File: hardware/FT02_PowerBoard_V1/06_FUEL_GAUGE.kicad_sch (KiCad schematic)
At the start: 0 parts

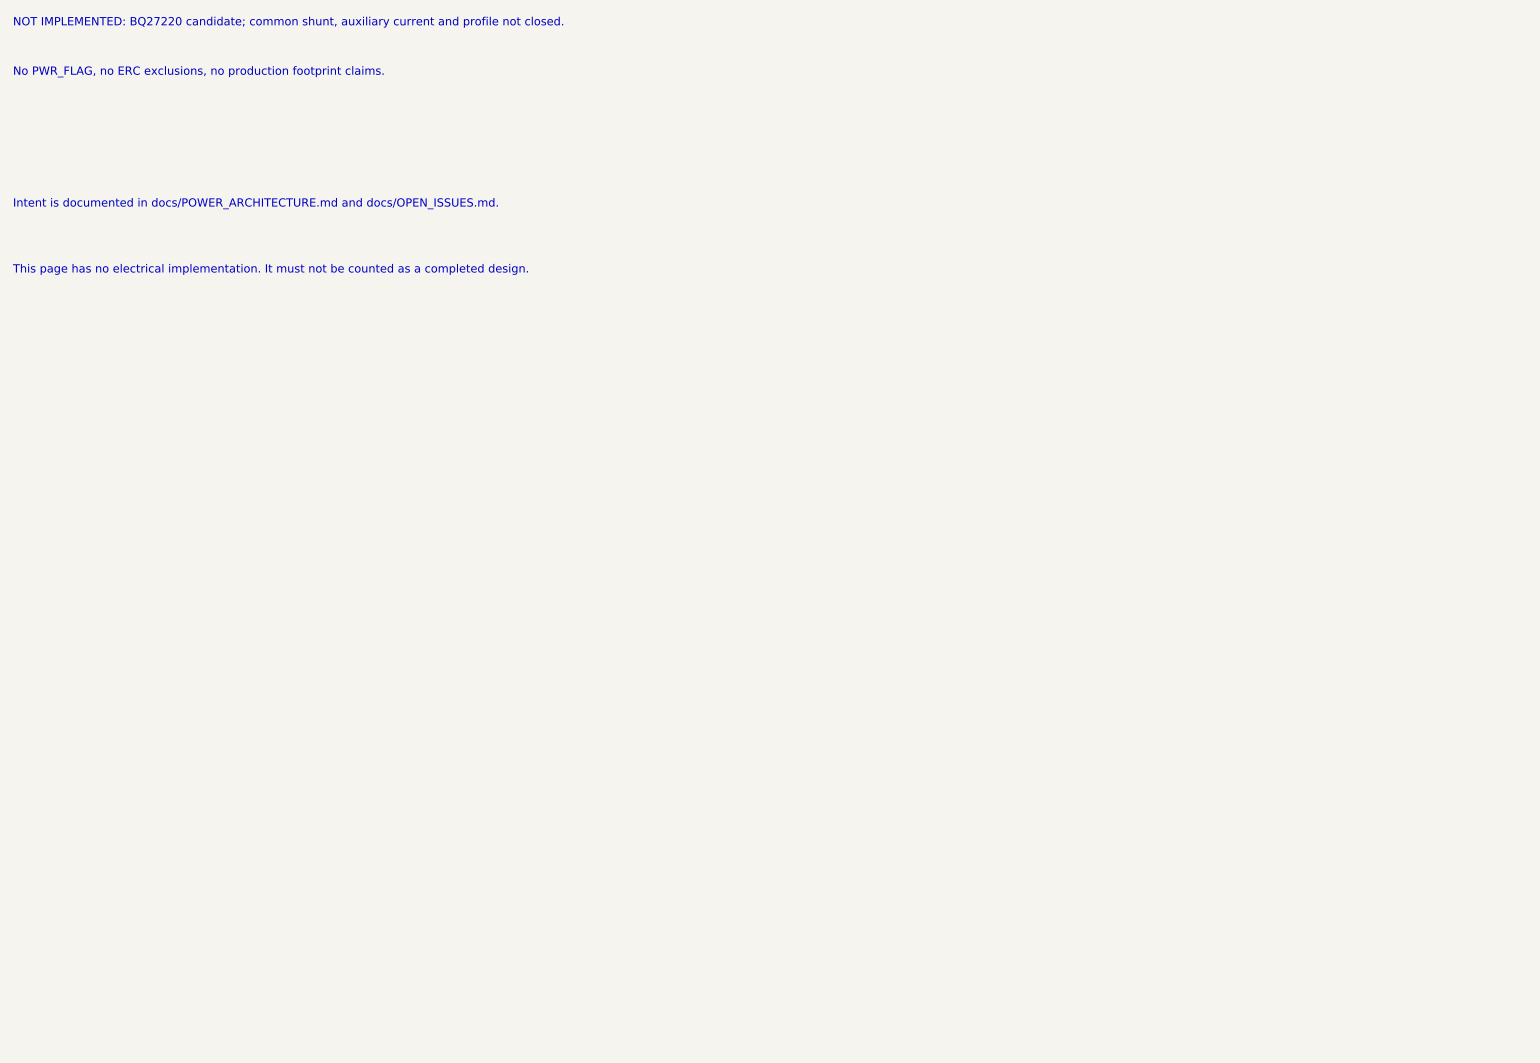
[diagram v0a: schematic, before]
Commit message: 采纳 FT02 电池来源限制并推进 Phase1 电量计参考电路
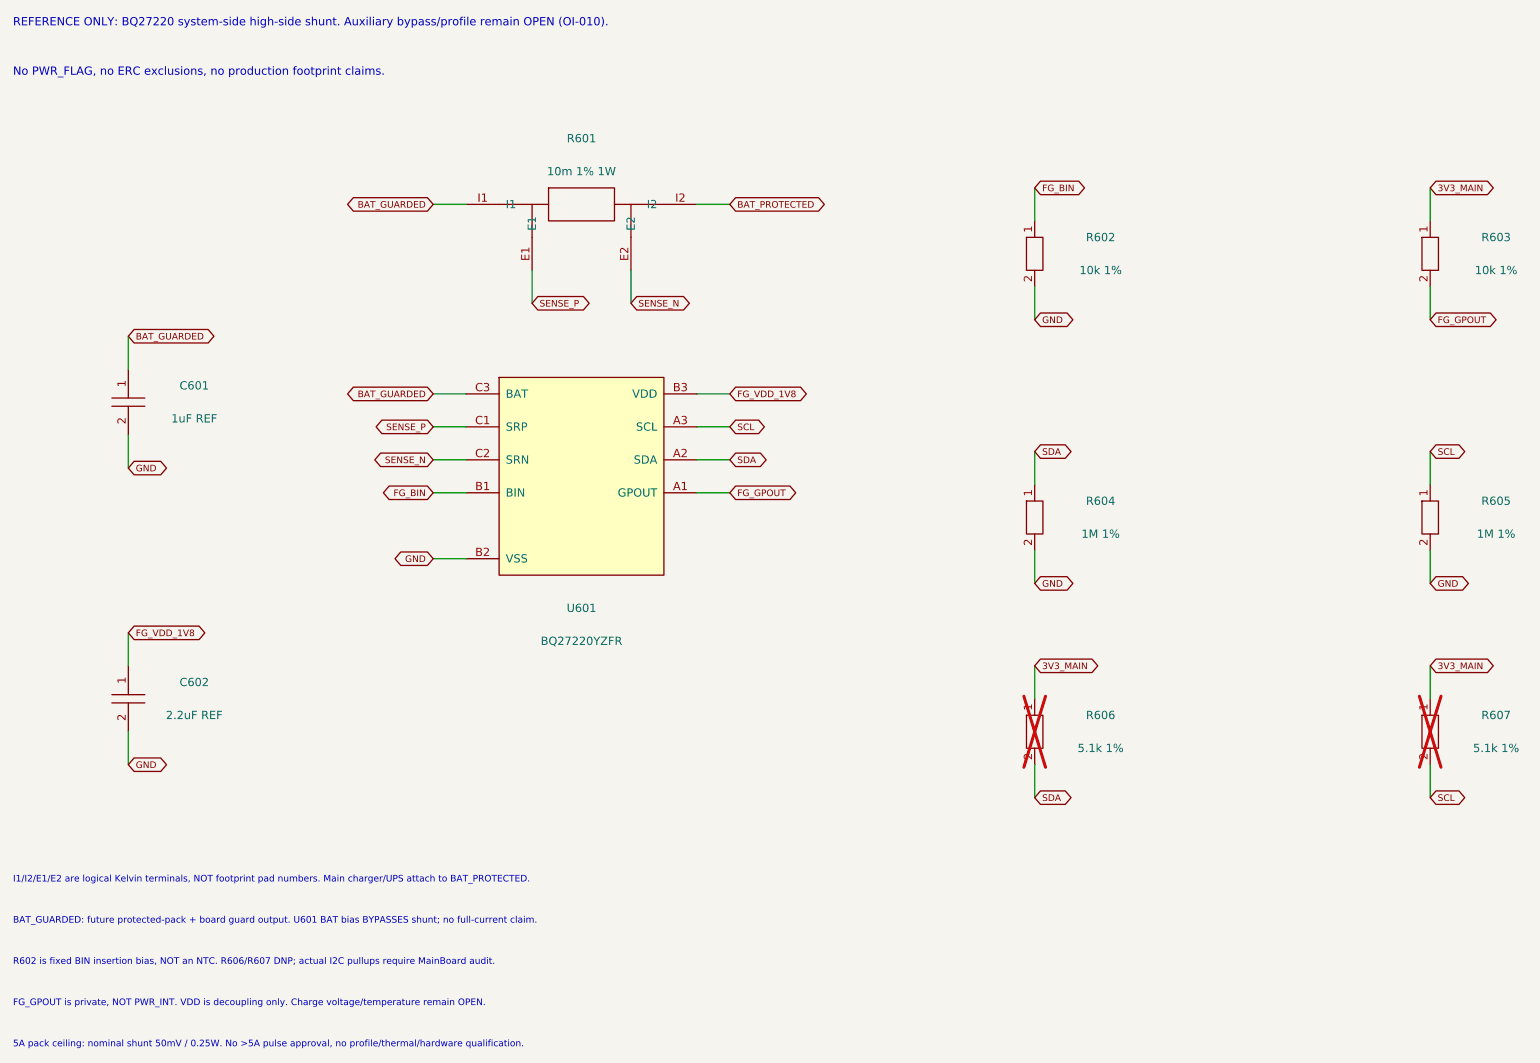
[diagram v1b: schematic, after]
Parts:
- added C601: 1uF REF, symbol FT02_Reference:C
- added C602: 2.2uF REF, symbol FT02_Reference:C
- added R601: 10m 1% 1W, symbol FT02_Reference:K4
- added R602, R603: 10k 1%, symbol FT02_Reference:R
- added R604, R605: 1M 1%, symbol FT02_Reference:R
- added R606, R607: 5.1k 1%, symbol FT02_Reference:R
- added U601: BQ27220YZFR, symbol FT02_Reference:BQ27220
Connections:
- new net 3V3_MAIN: R603.1, R606.1, R607.1
- new net BAT_GUARDED: C601.1, R601.I1, U601.C3 (BAT)
- new net BAT_PROTECTED: R601.I2
- new net FG_BIN: R602.1, U601.B1 (BIN)
- new net FG_GPOUT: R603.2, U601.A1 (GPOUT)
- new net FG_VDD_1V8: C602.1, U601.B3 (VDD)
- new net GND: C601.2, C602.2, R602.2, R604.2, R605.2, U601.B2 (VSS)
- new net SCL: R605.1, R607.2, U601.A3 (SCL)
- new net SDA: R604.1, R606.2, U601.A2 (SDA)
- new net SENSE_N: R601.E2, U601.C2 (SRN)
- new net SENSE_P: R601.E1, U601.C1 (SRP)
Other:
- note added: "5A pack ceiling: nominal shunt 50mV / 0.25W. No >5A pulse approval, no profile/thermal/hardware qualification."
- note added: "BAT_GUARDED: future protected-pack + board guard output. U601 BAT bias BYPASSES shunt; no full-current claim."
- note added: "FG_GPOUT is private, NOT PWR_INT. VDD is decoupling only. Charge voltage/temperature remain OPEN."
- note added: "I1/I2/E1/E2 are logical Kelvin terminals, NOT footprint pad numbers. Main charger/UPS attach to BAT_PROTECTED."
- note added: "R602 is fixed BIN insertion bias, NOT an NTC. R606/R607 DNP; actual I2C pullups require MainBoard audit."
- note added: "REFERENCE ONLY: BQ27220 system-side high-side shunt. Auxiliary bypass/profile remain OPEN (OI-010)."
- note removed: "Intent is documented in docs/POWER_ARCHITECTURE.md and docs/OPEN_ISSUES.md."
- note removed: "NOT IMPLEMENTED: BQ27220 candidate; common shunt, auxiliary current and profile not closed."
- note removed: "This page has no electrical implementation. It must not be counted as a completed design."
